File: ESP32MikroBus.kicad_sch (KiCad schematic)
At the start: 27 parts, among them IC1 ESP32-C6-WROOM-1-N4, IC2 AP7361C-33ER-13, J1 USB4105GFA120, J2 CON_HDR_MIKROBUS_SOCKET_TH, J3 Qwiic, U1 USBLC6-2P6

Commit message: PCB Layout v1.0 ready for verification by PCBWay
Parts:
- added J4: Conn_01x06, Connector_PinHeader_1.27mm:PinHeader_1x06_P1.27mm_Vertical, symbol Connector_Generic:Conn_01x06
- R7: now fitted
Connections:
- net +3V3 is gone; now on net +3.3V: R3.1
- net +5V: now also C5.1, F1.1, IC2.3 (IN), J2.15 (+5V), R7.1; no longer F1.2
- net +VBUS: now also F1.2; no longer F1.1
- net GND: now also S1.4, S1.6
- net MB_CS: now also IC1.12 (IO11)
- net MB_INT: now also IC1.4 (IO4)
- net MB_MISO: now also IC1.10 (IO8)
- net MB_MOSI: now also IC1.9 (IO1)
- net MB_PWM: now also IC1.26 (IO3)
- net MB_RST: now also IC1.5 (IO5)
- net MB_SCK: now also IC1.11 (IO10)
- net USR_LED: now also IC1.27 (IO2)
- net SPARE6: now reaches IC1.16 (IO18)
- net SPARE6: now also J4.6 (Pin_6)
- net SPARE5: now reaches IC1.17 (IO19)
- net SPARE5: now also J4.5 (Pin_5)
- net SPARE4: now reaches IC1.18 (IO20)
- net SPARE4: now also J4.4 (Pin_4)
- net SPARE3: now reaches IC1.19 (IO21)
- net SPARE3: now also J4.3 (Pin_3)
- net SPARE2: now reaches IC1.20 (IO22)
- net SPARE2: now also J4.2 (Pin_2)
- net SPARE1: now reaches IC1.21 (IO23)
- net SPARE1: now also J4.1 (Pin_1)
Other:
- moved on the sheet: C1, C2, C3, C4, C5, D1, D2, F1, IC2, J1, J2, R3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

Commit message: Minor update, mainly cosmetical + vbus not connected
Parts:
- removed J4: Conn_01x06, Connector_PinHeader_1.27mm:PinHeader_1x06_P1.27mm_Vertical, symbol Connector_Generic:Conn_01x06
- added J4: Conn_01x08, Connector_PinHeader_1.27mm:PinHeader_1x08_P1.27mm_Vertical, symbol Connector_Generic:Conn_01x08
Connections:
- net +3.3V: now also J4.1 (Pin_1)
- net +VBUS: now also U1.5 (VBUS)
- net GND: now also J4.8 (Pin_8)
- net SPARE1: now also J4.2 (Pin_2)
- net SPARE2: now also J4.3 (Pin_3)
- net SPARE3: now also J4.4 (Pin_4)
- net SPARE4: now also J4.5 (Pin_5)
- net SPARE5: now also J4.6 (Pin_6)
- net SPARE6: now also J4.7 (Pin_7)
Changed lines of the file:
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@@
 	(wire
 		(pts
+			(xy 127 88.9) (xy 121.92 88.9)
+		)
+		(stroke
+			(width 0)
+			(type default)
+		)
+	)
+	(wire
+		(pts
 			(xy 115.57 33.02) (xy 133.35 33.02)
 		)
@@
 	(wire
 		(pts
+			(xy 201.93 39.37) (xy 194.31 39.37)
+		)
+		(stroke
+			(width 0)
+			(type default)
+		)
+	)
+	(wire
+		(pts
 			(xy 109.22 124.46) (xy 109.22 133.35)
 		)
@@
 	(wire
 		(pts
+			(xy 121.92 88.9) (xy 121.92 85.09)
+		)
+		(stroke
+			(width 0)
+			(type default)
+		)
+	)
+	(wire
+		(pts
 			(xy 78.74 101.6) (xy 78.74 104.14)
 		)
@@
 	(wire
 		(pts
+			(xy 194.31 39.37) (xy 194.31 38.1)
+		)
+		(stroke
+			(width 0)
+			(type default)
+		)
+	)
+	(wire
+		(pts
 			(xy 66.04 76.2) (xy 82.55 76.2)
 		)
@@
 	(wire
 		(pts
+			(xy 127 106.68) (xy 121.92 106.68)
+		)
+		(stroke
+			(width 0)
+			(type default)
+		)
+	)
+	(wire
+		(pts
 			(xy 24.13 127) (xy 24.13 124.46)
 		)
@@
 	(wire
 		(pts
+			(xy 121.92 106.68) (xy 121.92 109.22)
+		)
+		(stroke
+			(width 0)
+			(type default)
+		)
+	)
+	(wire
+		(pts
 			(xy 53.34 147.32) (xy 53.34 152.4)
 		)
@@
 	(wire
 		(pts
-			(xy 198.12 36.83) (xy 198.12 39.37)
-		)
-		(stroke
-			(width 0)
-			(type default)
-		)
-	)
-	(wire
-		(pts
 			(xy 30.48 127) (xy 24.13 127)
 		)
@@
 	(wire
 		(pts
-			(xy 198.12 39.37) (xy 201.93 39.37)
-		)
-		(stroke
-			(width 0)
-			(type default)
-		)
-	)
-	(wire
-		(pts
 			(xy 226.06 143.51) (xy 236.22 143.51)
 		)
@@
 	)
 	(symbol
+		(lib_id "power:+5V")
+		(at 194.31 38.1 0)
+		(mirror y)
+		(unit 1)
+		(exclude_from_sim no)
+		(in_bom yes)
+		(on_board yes)
+		(dnp no)
+		(property "Reference" "#PWR02"
+			(at 194.31 41.91 0)
+			(effects
+				(font
+					(size 1.27 1.27)
+				)
+				(hide yes)
+			)
+		)
+		(property "Value" "+VBUS"
+			(at 194.056 32.512 0)
+			(effects
+				(font
+					(size 1.27 1.27)
+				)
+			)
+		)
+		(property "Footprint" ""
+			(at 194.31 38.1 0)
+			(effects
+				(font
+					(size 1.27 1.27)
+				)
+				(hide yes)
+			)
+		)
+		(property "Datasheet" ""
+			(at 194.31 38.1 0)
+			(effects
+				(font
+					(size 1.27 1.27)
+				)
+				(hide yes)
+			)
+		)
+		(property "Description" "Power symbol creates a global label with name \"+5V\""
+			(at 194.31 38.1 0)
+			(effects
+				(font
+					(size 1.27 1.27)
+				)
+				(hide yes)
+			)
+		)
+		(pin "1"
+		)
+		(instances
+			(project "ESP32MikroBus"
+				(path "/f1f042be-b4a8-4475-a6e6-c08e6b440fbe"
+					(reference "#PWR02")
+					(unit 1)
+				)
+			)
+		)
+	)
+	(symbol
 		(lib_id "power:GND")
 		(at 226.06 41.91 0)
@@
 	)
 	(symbol
+		(lib_id "Connector_Generic:Conn_01x08")
+		(at 132.08 96.52 0)
+		(unit 1)
+		(exclude_from_sim no)
+		(in_bom yes)
+		(on_board yes)
+		(dnp no)
+		(fields_autoplaced yes)
+		(property "Reference" "J4"
+			(at 134.62 96.5199 0)
+			(effects
+				(font
+					(size 1.27 1.27)
+				)
+				(justify left)
+			)
+		)
+		(property "Value" "Conn_01x08"
+			(at 134.62 99.0599 0)
+			(effects
+				(font
+					(size 1.27 1.27)
+				)
+				(justify left)
+			)
+		)
+		(property "Footprint" "Connector_PinHeader_1.27mm:PinHeader_1x08_P1.27mm_Vertical"
+			(at 132.08 96.52 0)
+			(effects
+				(font
+					(size 1.27 1.27)
+				)
+				(hide yes)
+			)
+		)
+		(property "Datasheet" "~"
+			(at 132.08 96.52 0)
+			(effects
+				(font
+					(size 1.27 1.27)
+				)
+				(hide yes)
+			)
+		)
+		(property "Description" "Generic connector, single row, 01x08, script generated (kicad-library-utils/schlib/autogen/connector/)"
+			(at 132.08 96.52 0)
+			(effects
+				(font
+					(size 1.27 1.27)
+				)
+				(hide yes)
+			)
+		)
+		(pin "6"
+		)
+		(pin "5"
+		)
+		(pin "2"
+		)
+		(pin "1"
+		)
+		(pin "7"
+		)
+		(pin "3"
+		)
+		(pin "4"
+		)
+		(pin "8"
+		)
+		(instances
+			(project ""
+				(path "/f1f042be-b4a8-4475-a6e6-c08e6b440fbe"
+					(reference "J4")
+					(unit 1)
+				)
+			)
+		)
+	)
+	(symbol
 		(lib_id "Device:R")
 		(at 236.22 80.01 90)
@@
 	)
 	(symbol
-		(lib_id "Connector_Generic:Conn_01x06")
-		(at 132.08 96.52 0)
+		(lib_id "power:GND")
+		(at 121.92 109.22 0)
 		(unit 1)
 		(exclude_from_sim no)
@@
 		(on_board yes)
 		(dnp no)
-		(fields_autoplaced yes)
-		(property "Reference" "J4"
-			(at 134.62 96.5199 0)
+		(property "Reference" "#PWR05"
+			(at 121.92 115.57 0)
 			(effects
 				(font
 					(size 1.27 1.27)
 				)
-				(justify left)
+				(hide yes)
 			)
 		)
-		(property "Value" "Conn_01x06"
-			(at 134.62 99.0599 0)
+		(property "Value" "GND"
+			(at 212.09 137.16 0)
 			(effects
 				(font
 					(size 1.27 1.27)
 				)
-				(justify left)
+				(hide yes)
 			)
 		)
-		(property "Footprint" "Connector_PinHeader_1.27mm:PinHeader_1x06_P1.27mm_Vertical"
-			(at 132.08 96.52 0)
+		(property "Footprint" ""
+			(at 121.92 109.22 0)
 			(effects
 				(font
@@
 			)
 		)
-		(property "Datasheet" "~"
-			(at 132.08 96.52 0)
+		(property "Datasheet" ""
+			(at 121.92 109.22 0)
 			(effects
 				(font
@@
 			)
 		)
-		(property "Description" "Generic connector, single row, 01x06, script generated (kicad-library-utils/schlib/autogen/connector/)"
-			(at 132.08 96.52 0)
+		(property "Description" ""
+			(at 121.92 109.22 0)
 			(effects
 				(font
@@
 			)
 		)
-		(pin "6"
-		)
 		(pin "1"
 		)
-		(pin "4"
-		)
-		(pin "2"
-		)
-		(pin "3"
-		)
-		(pin "5"
-		)
 		(instances
-			(project ""
+			(project "ESP32MikroBus"
 				(path "/f1f042be-b4a8-4475-a6e6-c08e6b440fbe"
-					(reference "J4")
+					(reference "#PWR05")
 					(unit 1)
 				)
@@
 	)
 	(symbol
-		(lib_id "power:GND")
-		(at 109.22 149.86 0)
+		(lib_id "power:+3.3V")
+		(at 121.92 85.09 0)
 		(unit 1)
 		(exclude_from_sim no)
@@
 		(dnp no)
 		(fields_autoplaced yes)
-		(property "Reference" "#PWR024"
-			(at 109.22 156.21 0)
+		(property "Reference" "#PWR029"
+			(at 121.92 88.9 0)
 			(effects
 				(font
@@
 			)
 		)
-		(property "Value" "GND"
-			(at 109.22 154.94 0)
+		(property "Value" "+3.3V"
+			(at 121.92 80.01 0)
 			(effects
 				(font
@@
 		)
 		(property "Footprint" ""
-			(at 109.22 149.86 0)
+			(at 121.92 85.09 0)
 			(effects
 				(font
@@
 		)
 		(property "Datasheet" ""
-			(at 109.22 149.86 0)
+			(at 121.92 85.09 0)
 			(effects
 				(font
@@
 		)
 		(property "Description" ""
-			(at 109.22 149.86 0)
+			(at 121.92 85.09 0)
 			(effects
 				(font
@@
 			(project "ESP32MikroBus"
 				(path "/f1f042be-b4a8-4475-a6e6-c08e6b440fbe"
-					(reference "#PWR024")
+					(reference "#PWR029")
 					(unit 1)
 				)
@@
 	)
 	(symbol
-		(lib_name "+5V_3")
-		(lib_id "power:+5V")
-		(at 198.12 36.83 0)
+		(lib_id "power:GND")
+		(at 109.22 149.86 0)
 		(unit 1)
 		(exclude_from_sim no)
@@
 		(on_board yes)
 		(dnp no)
-		(property "Reference" "#PWR05"
-			(at 198.12 40.64 0)
+		(fields_autoplaced yes)
+		(property "Reference" "#PWR024"
+			(at 109.22 156.21 0)
 			(effects
 				(font
@@
 			)
 		)
-		(property "Value" "+5V"
-			(at 198.12 31.75 0)
+		(property "Value" "GND"
+			(at 109.22 154.94 0)
 			(effects
 				(font
@@
 		)
 		(property "Footprint" ""
-			(at 198.12 36.83 0)
+			(at 109.22 149.86 0)
 			(effects
 				(font
@@
 		)
 		(property "Datasheet" ""
-			(at 198.12 36.83 0)
+			(at 109.22 149.86 0)
 			(effects
 				(font
@@
 		)
 		(property "Description" ""
-			(at 198.12 36.83 0)
+			(at 109.22 149.86 0)
 			(effects
 				(font
@@
 			(project "ESP32MikroBus"
 				(path "/f1f042be-b4a8-4475-a6e6-c08e6b440fbe"
-					(reference "#PWR05")
+					(reference "#PWR024")
 					(unit 1)
 				)

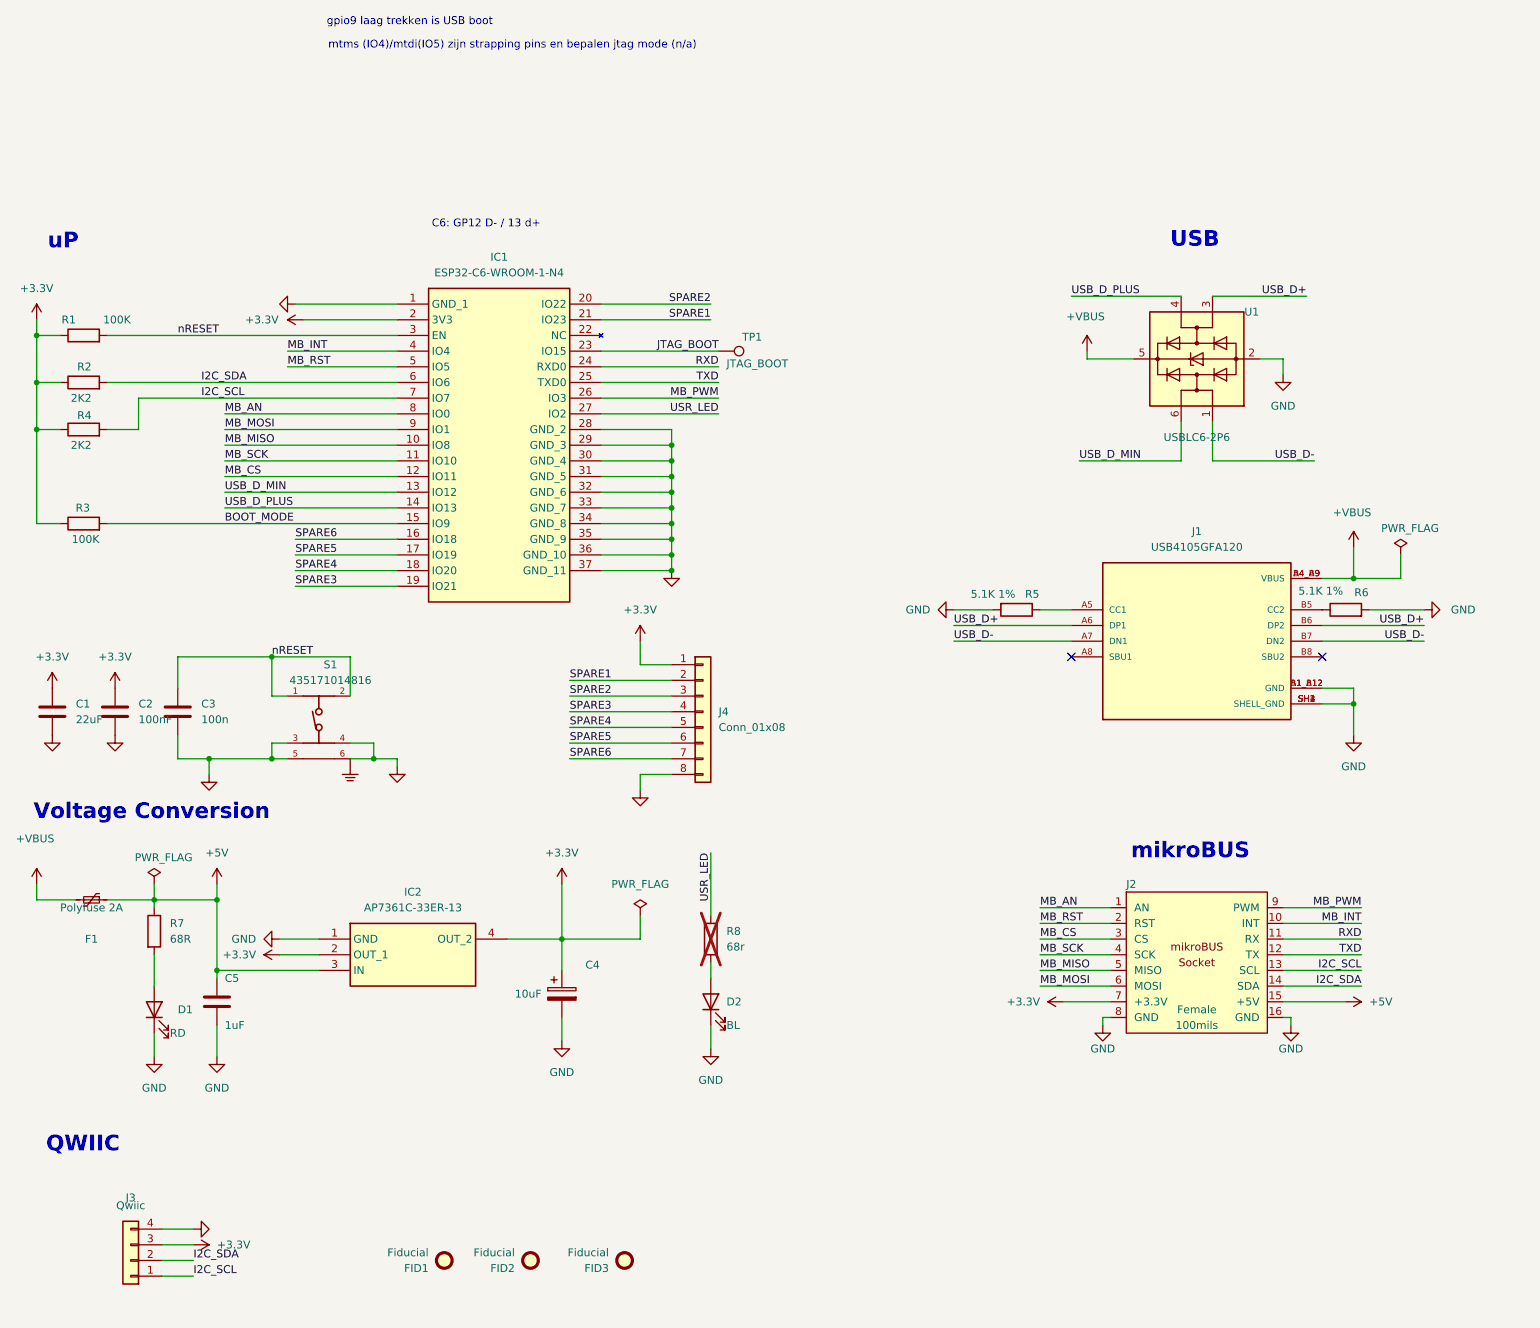
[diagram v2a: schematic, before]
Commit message: Changed c1 to 10uF, more attention to power traces, fixed copper plane and qwiic connector
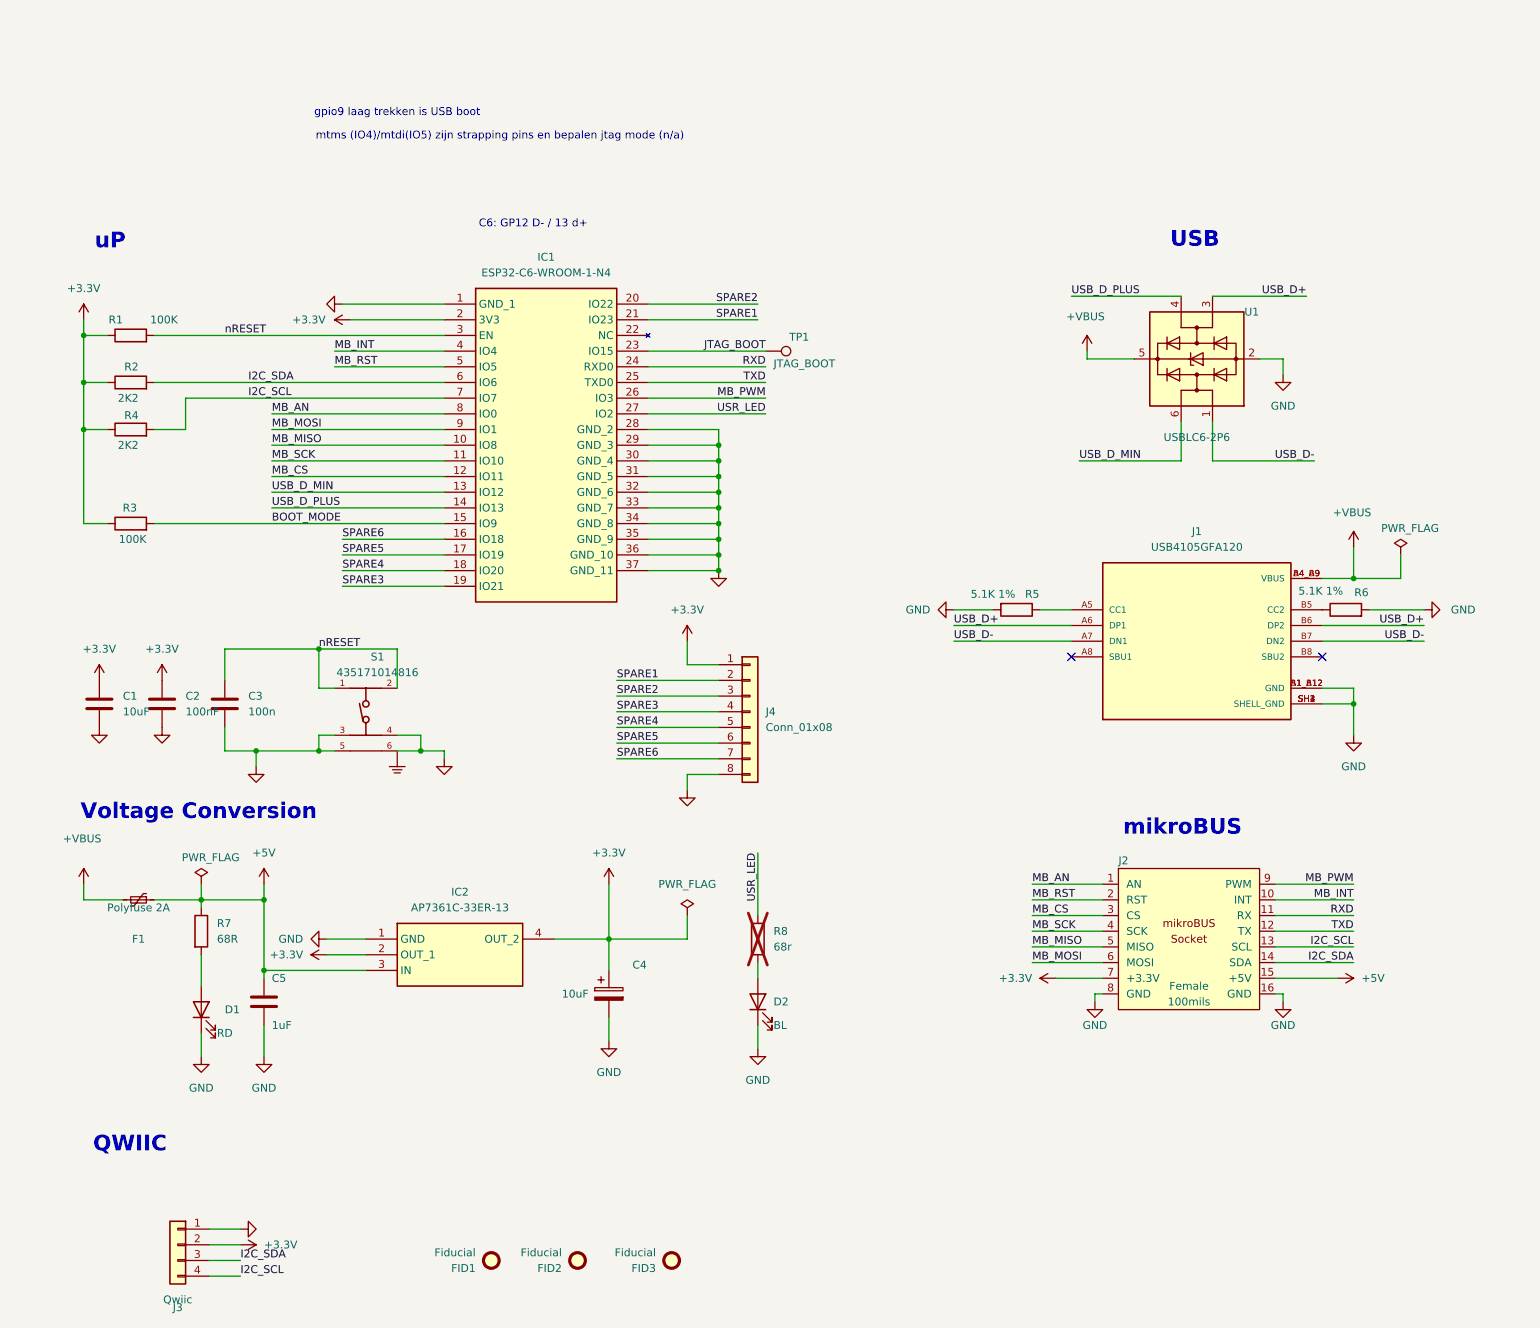
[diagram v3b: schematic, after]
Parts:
- C1: value 22uF -> 10uF
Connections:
- net +3.3V: now also J3.2 (Pin_2); no longer J3.3 (Pin_3)
- net GND: now also J3.1 (Pin_1); no longer J3.4 (Pin_4)
- net I2C_SCL: now also J3.4 (Pin_4); no longer J3.1 (Pin_1)
- net I2C_SDA: now also J3.3 (Pin_3); no longer J3.2 (Pin_2)
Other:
- moved on the sheet: C1, C2, C3, C4, C5, D1, D2, F1, FID1, FID2, FID3, IC1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
